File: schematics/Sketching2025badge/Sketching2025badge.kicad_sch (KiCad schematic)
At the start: 20 parts, among them J1 Conn_02x03, J2 Conn_01x04_Pin, U1 ATtiny816-M, U2 BH-AAA-A1AJ001, U3 BH-AAA-A1AJ001

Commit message: almost routed, difficult getting through the maze of the B.Mask
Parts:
- added LED4, LED5, LED6: SK6812SIDE, todbot_stuff:LED-SMD_4P-L4.0-W1.6-L, symbol todbot_stuff:SK6812SIDE
- added SW1, SW2, SW3: Capacitive_Button, todbot_stuff:Pad-CapTouch-10mm-roundrect-nosilk, symbol todbot_stuff:Capacitive_Button
- added TP1, TP2, TP3, TP4: Sewable, TestPoint:TestPoint_Keystone_5010-5014_Multipurpose, symbol Connector:TestPoint
- J1: footprint 4ms_Connector:Pins_2x03_2.54mm_TH -> Connector_PinSocket_2.54mm:PinSocket_2x03_P2.54mm_Vertical
- renumbered U2 to BAT1, U3 to BAT2, LED3 to LED2, LED2 to LED3
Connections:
- net GND: now also J1.2 (+12V), LED4.4 (GND), LED5.4 (GND), LED6.4 (GND), TP2.1
- net RXD: now also J1.6 (GND), TP4.1
- net SCL: now also J1.4 (GND)
- net SDA: now also J1.3 (GND)
- net TOUCH0: now also SW1.1 (A)
- net TOUCH1: now also SW2.1 (A)
- net TOUCH2: now also SW3.1 (A)
- net TXD: now also J1.5 (GND), TP3.1
- net VCC: now also BAT1.2 (+), J1.1 (+12V), LED4.2 (VDD), LED5.2 (VDD), LED6.2 (VDD), TP1.1
- net PA3: now reaches U1.2 (PA3)
- net PA7: now reaches U1.8 (PA7)
- net PB5: now reaches U1.9 (PB5)
- net TX: now reaches J2.4 (Pin_4), R7.1
- net at LED3.3 (DOUT): now also LED4.1 (DIN)
- new net: LED5.3 (DOUT), LED6.1 (DIN)
- new net: LED4.3 (DOUT), LED5.1 (DIN)
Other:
- note added: "LEDs originally routed 1,3,2 instead of 1,2,3 because DIN/DOUT on these SK6812SIDE want CCW routing"
- note removed: "LEDs routed 1,3,2 instead of 1,2,3 because DIN/DOUT on these SK6812SIDE want CCW routing"
- moved on the sheet: BAT1, BAT2, J1, LED1, LED2, LED3, R9

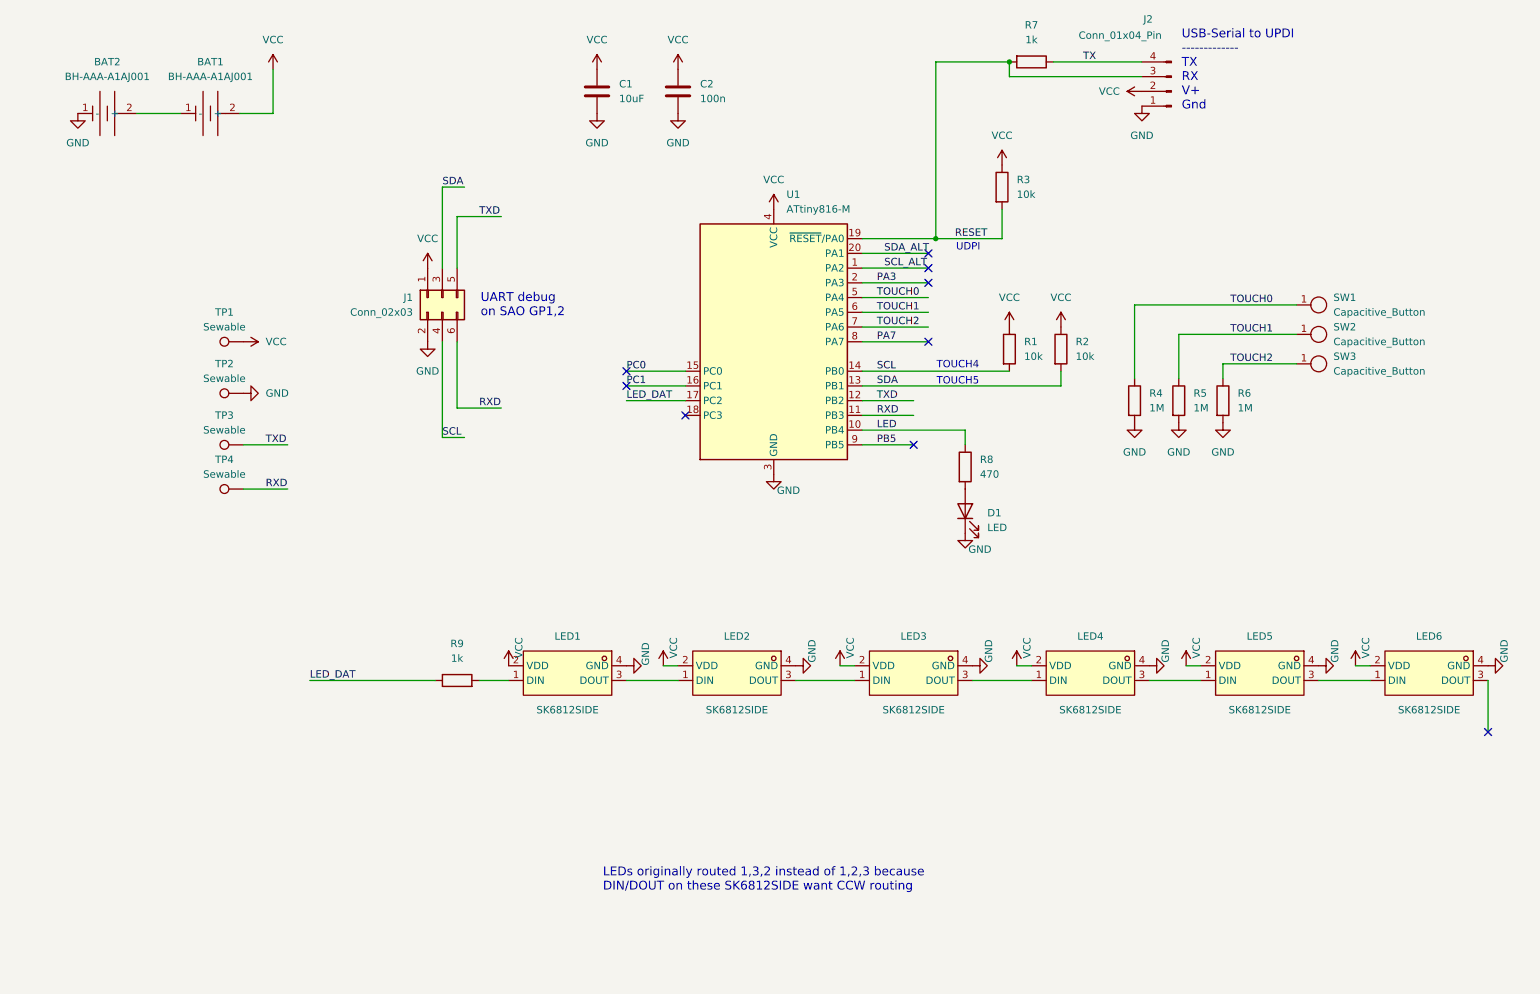
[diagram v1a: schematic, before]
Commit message: first version routed, not pass drc yet
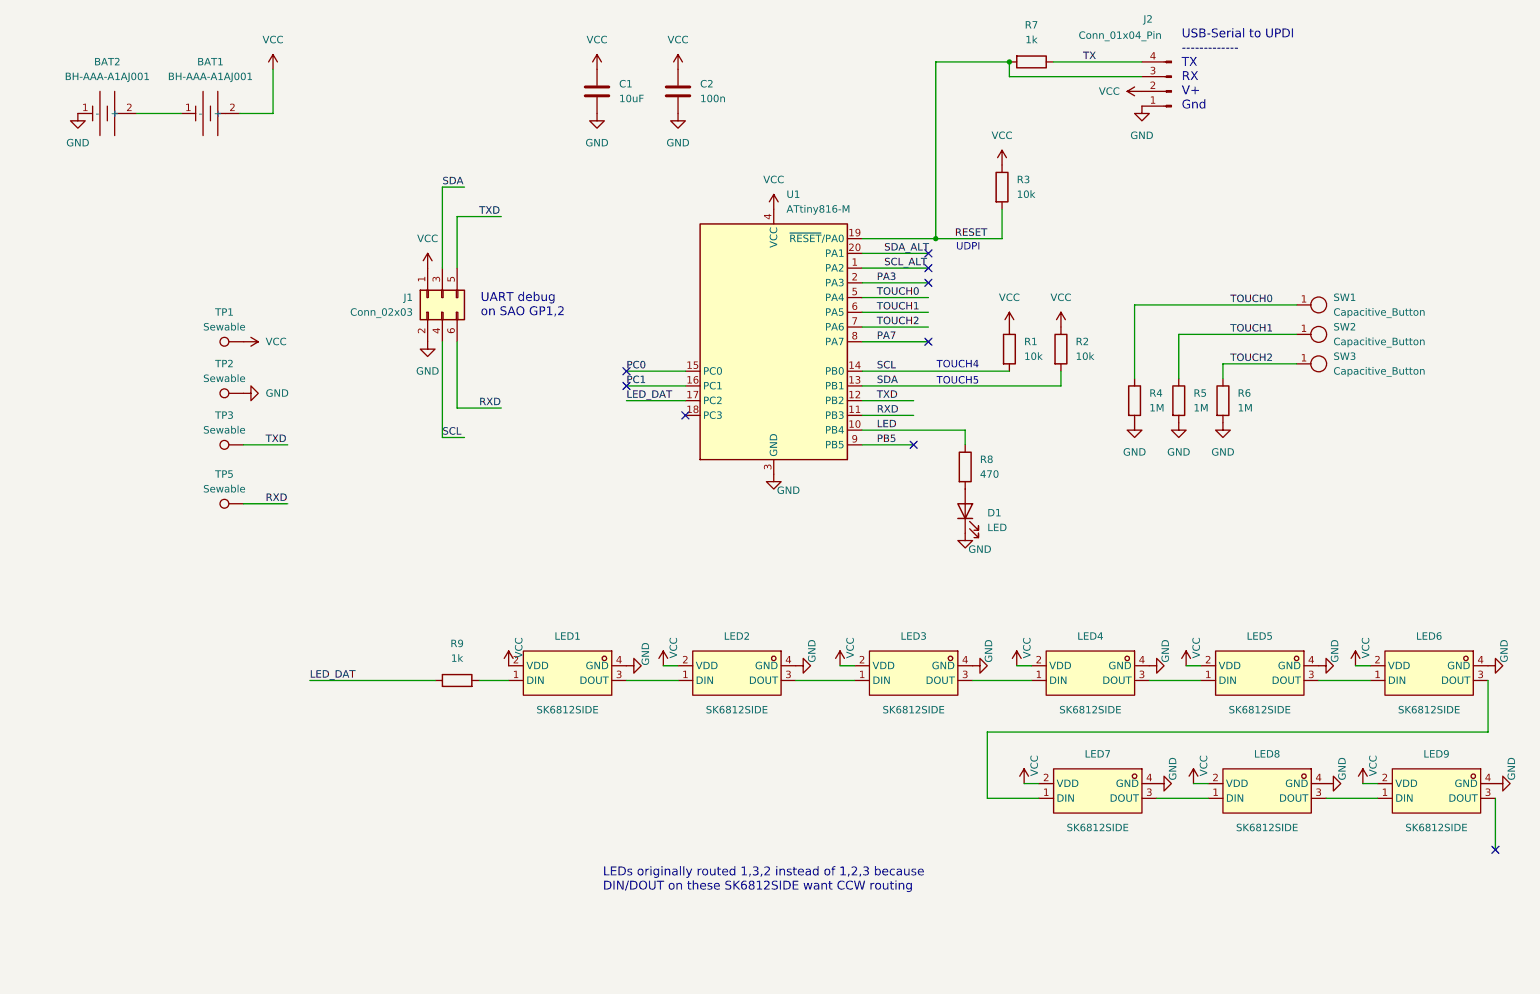
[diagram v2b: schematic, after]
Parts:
- removed TP4: Sewable, TestPoint:TestPoint_Keystone_5010-5014_Multipurpose, symbol Connector:TestPoint
- added LED7, LED8, LED9: SK6812SIDE, todbot_stuff:LED-SMD_4P-L4.0-W1.6-L, symbol todbot_stuff:SK6812SIDE
- added TP5: Sewable, todbot_stuff:Lilypad-BUTTONHOLE, symbol Connector:TestPoint
- TP1, TP2, TP3: footprint TestPoint:TestPoint_Keystone_5010-5014_Multipurpose -> todbot_stuff:Lilypad-BUTTONHOLE
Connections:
- net GND: now also LED7.4 (GND), LED8.4 (GND), LED9.4 (GND)
- net RXD: now also TP5.1
- net VCC: now also LED7.2 (VDD), LED8.2 (VDD), LED9.2 (VDD)
- net at LED6.3 (DOUT): now also LED7.1 (DIN)
- new net: LED7.3 (DOUT), LED8.1 (DIN)
- new net: LED8.3 (DOUT), LED9.1 (DIN)

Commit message: routed, mostly pass drc
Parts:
- added H1: MountingHole, MountingHole:MountingHole_6.4mm_M6, symbol Mechanical:MountingHole
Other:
- moved on the sheet: TP1, TP2, TP3, TP5
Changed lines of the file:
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@@
 	(text "LEDs originally routed 1,3,2 instead of 1,2,3 because\nDIN/DOUT on these SK6812SIDE want CCW routing"
 		(exclude_from_sim no)
-		(at 121.666 169.418 0)
+		(at 105.156 179.07 0)
 		(effects
 			(font
@@
 	(wire
 		(pts
-			(xy 59.69 106.68) (xy 67.31 106.68)
+			(xy 54.61 90.17) (xy 62.23 90.17)
 		)
 		(stroke
@@
 	(wire
 		(pts
-			(xy 59.69 96.52) (xy 67.31 96.52)
+			(xy 54.61 80.01) (xy 62.23 80.01)
 		)
 		(stroke
@@
 	)
 	(label "TXD"
-		(at 63.5 96.52 0)
+		(at 58.42 80.01 0)
 		(effects
 			(font
@@
 	)
 	(label "RXD"
-		(at 63.5 106.68 0)
+		(at 58.42 90.17 0)
 		(effects
 			(font
@@
 	(symbol
 		(lib_id "power:GND")
-		(at 59.69 87.63 90)
+		(at 54.61 71.12 90)
 		(unit 1)
 		(exclude_from_sim no)
@@
 		(fields_autoplaced yes)
 		(property "Reference" "#PWR032"
-			(at 66.04 87.63 0)
+			(at 60.96 71.12 0)
 			(effects
 				(font
@@
 		)
 		(property "Value" "GND"
-			(at 63.5 87.6299 90)
+			(at 58.42 71.1199 90)
 			(effects
 				(font
@@
 		)
 		(property "Footprint" ""
-			(at 59.69 87.63 0)
+			(at 54.61 71.12 0)
 			(effects
 				(font
@@
 		)
 		(property "Datasheet" ""
-			(at 59.69 87.63 0)
+			(at 54.61 71.12 0)
 			(effects
 				(font
@@
 		)
 		(property "Description" "Power symbol creates a global label with name \"GND\" , ground"
-			(at 59.69 87.63 0)
+			(at 54.61 71.12 0)
 			(effects
 				(font
@@
 	(symbol
 		(lib_id "power:VCC")
-		(at 59.69 78.74 270)
+		(at 54.61 62.23 270)
 		(unit 1)
 		(exclude_from_sim no)
@@
 		(fields_autoplaced yes)
 		(property "Reference" "#PWR033"
-			(at 55.88 78.74 0)
+			(at 50.8 62.23 0)
 			(effects
 				(font
@@
 		)
 		(property "Value" "VCC"
-			(at 63.5 78.7399 90)
+			(at 58.42 62.2299 90)
 			(effects
 				(font
@@
 		)
 		(property "Footprint" ""
-			(at 59.69 78.74 0)
+			(at 54.61 62.23 0)
 			(effects
 				(font
@@
 		)
 		(property "Datasheet" ""
-			(at 59.69 78.74 0)
+			(at 54.61 62.23 0)
 			(effects
 				(font
@@
 		)
 		(property "Description" "Power symbol creates a global label with name \"VCC\""
-			(at 59.69 78.74 0)
+			(at 54.61 62.23 0)
 			(effects
 				(font
@@
 	)
 	(symbol
+		(lib_id "Mechanical:MountingHole")
+		(at 21.59 186.69 0)
+		(unit 1)
+		(exclude_from_sim no)
+		(in_bom no)
+		(on_board yes)
+		(dnp no)
+		(fields_autoplaced yes)
+		(property "Reference" "H1"
+			(at 24.13 185.4199 0)
+			(effects
+				(font
+					(size 1.27 1.27)
+				)
+				(justify left)
+			)
+		)
+		(property "Value" "MountingHole"
+			(at 24.13 187.9599 0)
+			(effects
+				(font
+					(size 1.27 1.27)
+				)
+				(justify left)
+			)
+		)
+		(property "Footprint" "MountingHole:MountingHole_6.4mm_M6"
+			(at 21.59 186.69 0)
+			(effects
+				(font
+					(size 1.27 1.27)
+				)
+				(hide yes)
+			)
+		)
+		(property "Datasheet" "~"
+			(at 21.59 186.69 0)
+			(effects
+				(font
+					(size 1.27 1.27)
+				)
+				(hide yes)
+			)
+		)
+		(property "Description" "Mounting Hole without connection"
+			(at 21.59 186.69 0)
+			(effects
+				(font
+					(size 1.27 1.27)
+				)
+				(hide yes)
+			)
+		)
+		(instances
+			(project ""
+				(path "/598c645d-45d3-4f84-85f8-bbbc5b47d1f0"
+					(reference "H1")
+					(unit 1)
+				)
+			)
+		)
+	)
+	(symbol
 		(lib_id "power:GND")
 		(at 185.42 134.62 90)
@@
 	(symbol
 		(lib_id "Connector:TestPoint")
-		(at 59.69 87.63 90)
+		(at 54.61 71.12 90)
 		(unit 1)
 		(exclude_from_sim no)
@@
 		(fields_autoplaced yes)
 		(property "Reference" "TP2"
-			(at 56.388 82.55 90)
+			(at 51.308 66.04 90)
 			(effects
 				(font
@@
 		)
 		(property "Value" "Sewable"
-			(at 56.388 85.09 90)
+			(at 51.308 68.58 90)
 			(effects
 				(font
@@
 		)
 		(property "Footprint" "todbot_stuff:Lilypad-BUTTONHOLE"
-			(at 59.69 82.55 0)
+			(at 54.61 66.04 0)
 			(effects
 				(font
@@
 		)
 		(property "Datasheet" "~"
-			(at 59.69 82.55 0)
+			(at 54.61 66.04 0)
 			(effects
 				(font
@@
 		)
 		(property "Description" "test point"
-			(at 59.69 87.63 0)
+			(at 54.61 71.12 0)
 			(effects
 				(font
@@
 	(symbol
 		(lib_id "Connector:TestPoint")
-		(at 59.69 78.74 90)
+		(at 54.61 62.23 90)
 		(unit 1)
 		(exclude_from_sim no)
@@
 		(fields_autoplaced yes)
 		(property "Reference" "TP1"
-			(at 56.388 73.66 90)
+			(at 51.308 57.15 90)
 			(effects
 				(font
@@
 		)
 		(property "Value" "Sewable"
-			(at 56.388 76.2 90)
+			(at 51.308 59.69 90)
 			(effects
 				(font
@@
 		)
 		(property "Footprint" "todbot_stuff:Lilypad-BUTTONHOLE"
-			(at 59.69 73.66 0)
+			(at 54.61 57.15 0)
 			(effects
 				(font
@@
 		)
 		(property "Datasheet" "~"
-			(at 59.69 73.66 0)
+			(at 54.61 57.15 0)
 			(effects
 				(font
@@
 		)
 		(property "Description" "test point"
-			(at 59.69 78.74 0)
+			(at 54.61 62.23 0)
 			(effects
 				(font
@@
 	(symbol
 		(lib_id "Connector:TestPoint")
-		(at 59.69 106.68 90)
+		(at 54.61 90.17 90)
 		(unit 1)
 		(exclude_from_sim no)
@@
 		(fields_autoplaced yes)
 		(property "Reference" "TP5"
-			(at 56.388 101.6 90)
+			(at 51.308 85.09 90)
 			(effects
 				(font
@@
 		)
 		(property "Value" "Sewable"
-			(at 56.388 104.14 90)
+			(at 51.308 87.63 90)
 			(effects
 				(font
@@
 		)
 		(property "Footprint" "todbot_stuff:Lilypad-BUTTONHOLE"
-			(at 59.69 101.6 0)
+			(at 54.61 85.09 0)
 			(effects
 				(font
@@
 		)
 		(property "Datasheet" "~"
-			(at 59.69 101.6 0)
+			(at 54.61 85.09 0)
 			(effects
 				(font
@@
 		)
 		(property "Description" "test point"
-			(at 59.69 106.68 0)
+			(at 54.61 90.17 0)
 			(effects
 				(font
@@
 	(symbol
 		(lib_id "Connector:TestPoint")
-		(at 59.69 96.52 90)
+		(at 54.61 80.01 90)
 		(unit 1)
 		(exclude_from_sim no)
@@
 		(fields_autoplaced yes)
 		(property "Reference" "TP3"
-			(at 56.388 91.44 90)
+			(at 51.308 74.93 90)
 			(effects
 				(font
@@
 		)
 		(property "Value" "Sewable"
-			(at 56.388 93.98 90)
+			(at 51.308 77.47 90)
 			(effects
 				(font
@@
 		)
 		(property "Footprint" "todbot_stuff:Lilypad-BUTTONHOLE"
-			(at 59.69 91.44 0)
+			(at 54.61 74.93 0)
 			(effects
 				(font
@@
 		)
 		(property "Datasheet" "~"
-			(at 59.69 91.44 0)
+			(at 54.61 74.93 0)
 			(effects
 				(font
@@
 		)
 		(property "Description" "test point"
-			(at 59.69 96.52 0)
+			(at 54.61 80.01 0)
 			(effects
 				(font

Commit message: added bypass caps and switch
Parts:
- removed TP5: Sewable, todbot_stuff:Lilypad-BUTTONHOLE, symbol Connector:TestPoint
- added C10, C11, C3, C4, C5, C6, C7, C8, C9: 100n, Resistor_SMD:R_0603_1608Metric, symbol Device:C
- added SW10: SSSS811101, easyeda2kicad:SW-SMD_SSSS811101, symbol easyeda2kicad:SSSS811101
- added TP4: Sewable, todbot_stuff:Lilypad-BUTTONHOLE, symbol Connector:TestPoint
- added TP6, TP7, TP8: TestPoint, TestPoint:TestPoint_Pad_D1.5mm, symbol Connector:TestPoint
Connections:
- net GND: now also C10.2, C11.2, C3.2, C4.2, C5.2, C6.2, C7.2, C8.2, C9.2, SW10.4, SW10.5, SW10.6, SW10.7
- net LED_DAT: now also TP6.1
- net RXD: now also TP4.1
- net SCL_ALT: now also TP8.1
- net SDA_ALT: now also TP7.1
- net TOUCH0: now also U1.7 (PA6); no longer U1.5 (PA4)
- net TOUCH2: now also U1.5 (PA4); no longer U1.7 (PA6)
- net VCC: now also C10.1, C11.1, C3.1, C4.1, C5.1, C6.1, C7.1, C8.1, C9.1, SW10.2; no longer BAT1.2 (+)
- new net: BAT1.2 (+), SW10.1
- no-connect marks 9 -> 8

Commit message: first version to production
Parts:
- C1: LCSC Part (none) -> C434425
- C10, C11, C2, C3, C4, C5, C6, C7, C8, C9: LCSC Part (none) -> C1590
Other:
- note added: "USB-Serial to UPDI ------------- TX RX 3v3 Gnd"
- note removed: "USB-Serial to UPDI ------------- TX RX V+ Gnd"
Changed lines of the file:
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@@
 		)
 	)
-	(text "USB-Serial to UPDI\n-------------\nTX\nRX\nV+\nGnd\n"
+	(text "USB-Serial to UPDI\n-------------\nTX\nRX\n3v3\nGnd\n"
 		(exclude_from_sim no)
 		(at 221.488 24.892 0)
@@
 			)
 		)
+		(property "LCSC Part" "C1590"
+			(at 125.73 158.75 0)
+			(effects
+				(font
+					(size 1.27 1.27)
+				)
+				(hide yes)
+			)
+		)
 		(pin "2"
 		)
@@
 			)
 		)
+		(property "LCSC Part" "C1590"
+			(at 63.5 158.75 0)
+			(effects
+				(font
+					(size 1.27 1.27)
+				)
+				(hide yes)
+			)
+		)
 		(pin "2"
 		)
@@
 			)
 		)
+		(property "LCSC Part" "C1590"
+			(at 138.43 158.75 0)
+			(effects
+				(font
+					(size 1.27 1.27)
+				)
+				(hide yes)
+			)
+		)
 		(pin "2"
 		)
@@
 			)
 		)
+		(property "LCSC Part" "C1590"
+			(at 114.3 158.75 0)
+			(effects
+				(font
+					(size 1.27 1.27)
+				)
+				(hide yes)
+			)
+		)
 		(pin "2"
 		)
@@
 			)
 		)
+		(property "LCSC Part" "C1590"
+			(at 52.07 158.75 0)
+			(effects
+				(font
+					(size 1.27 1.27)
+				)
+				(hide yes)
+			)
+		)
 		(pin "2"
 		)
@@
 			)
 		)
+		(property "LCSC Part" "C1590"
+			(at 100.33 158.75 0)
+			(effects
+				(font
+					(size 1.27 1.27)
+				)
+				(hide yes)
+			)
+		)
 		(pin "2"
 		)
@@
 			)
 		)
+		(property "LCSC Part" "C434425"
+			(at 120.65 35.56 0)
+			(effects
+				(font
+					(size 1.27 1.27)
+				)
+				(hide yes)
+			)
+		)
 		(pin "2"
 		)
@@
 			)
 		)
+		(property "LCSC Part" "C1590"
+			(at 134.62 35.56 0)
+			(effects
+				(font
+					(size 1.27 1.27)
+				)
+				(hide yes)
+			)
+		)
 		(pin "2"
 		)
@@
 			)
 		)
+		(property "LCSC Part" "C1590"
+			(at 149.86 158.75 0)
+			(effects
+				(font
+					(size 1.27 1.27)
+				)
+				(hide yes)
+			)
+		)
 		(pin "2"
 		)
@@
 			)
 		)
+		(property "LCSC Part" "C1590"
+			(at 76.2 158.75 0)
+			(effects
+				(font
+					(size 1.27 1.27)
+				)
+				(hide yes)
+			)
+		)
 		(pin "2"
 		)
@@
 			(at 87.63 158.75 0)
 			(effects
+				(font
+					(size 1.27 1.27)
+				)
+				(hide yes)
+			)
+		)
+		(property "LCSC Part" "C1590"
+			(at 87.63 158.75 0)
+			(effects
